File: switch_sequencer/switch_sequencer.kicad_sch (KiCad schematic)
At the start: 0 parts

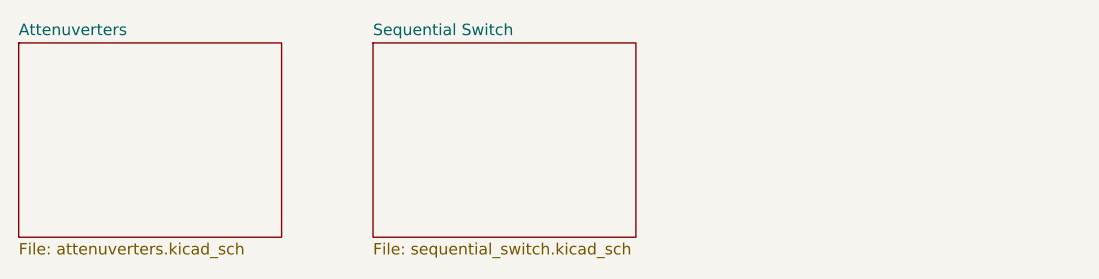
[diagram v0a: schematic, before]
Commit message: Updated schematic of sample and hold, attenuveters, sequential switch
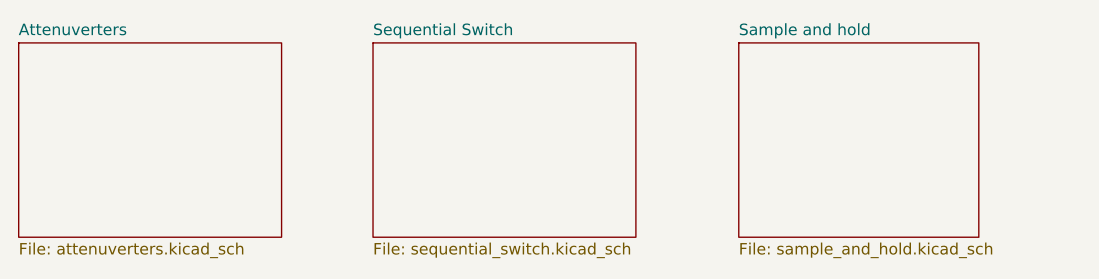
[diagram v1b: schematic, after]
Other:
- added sheet Sample and hold (sample_and_hold.kicad_sch)
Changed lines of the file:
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@@
+	)
+	(sheet
+		(at 137.16 62.23)
+		(size 26.67 21.59)
+		(fields_autoplaced yes)
+		(stroke
+			(width 0.1524)
+			(type solid)
+		)
+		(fill
+			(color 0 0 0 0.0000)
+		)
+		(property "Sheetname" "Sample and hold"
+			(at 137.16 61.5184 0)
+			(effects
+				(font
+					(size 1.27 1.27)
+				)
+				(justify left bottom)
+			)
+		)
+		(property "Sheetfile" "sample_and_hold.kicad_sch"
+			(at 137.16 84.4046 0)
+			(effects
+				(font
+					(size 1.27 1.27)
+				)
+				(justify left top)
+			)
+		)
+		(instances
+			(project "switch_sequencer"
+				(path "/1090b42d-0526-4901-ae26-1a4493d10820"
+					(page "8")
+				)
+			)
+		)
 	)
 	(sheet
